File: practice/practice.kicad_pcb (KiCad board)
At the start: 2 copper layers, 27 x 22 mm, 5 parts

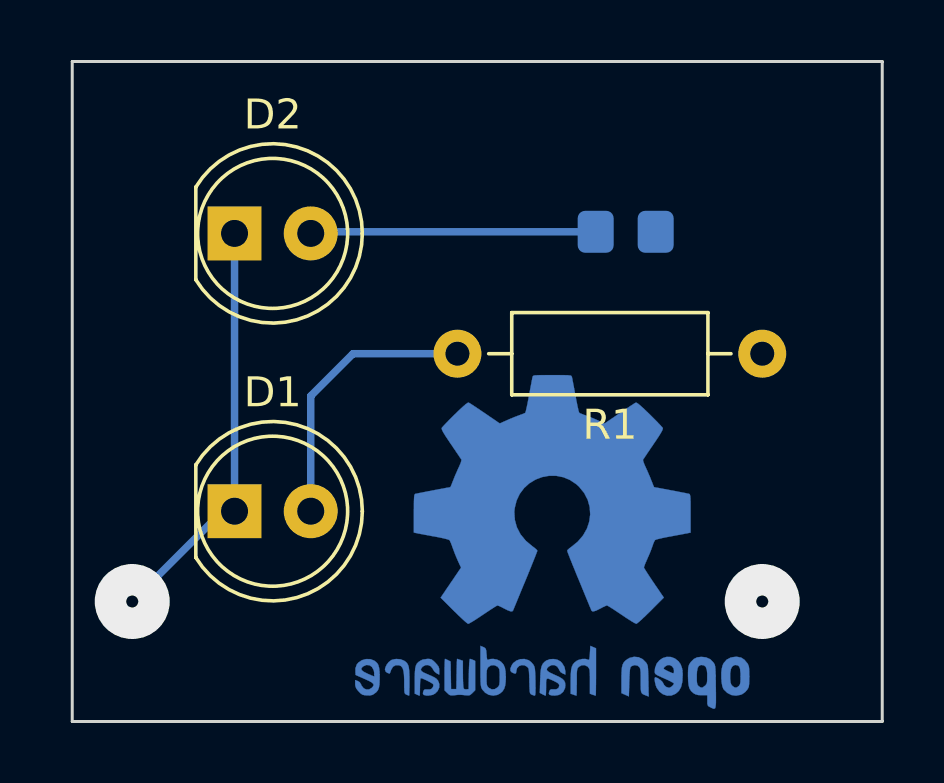
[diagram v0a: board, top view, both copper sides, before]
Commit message: 新增'UNO V3'資料夾 新增'learning project'資料夾
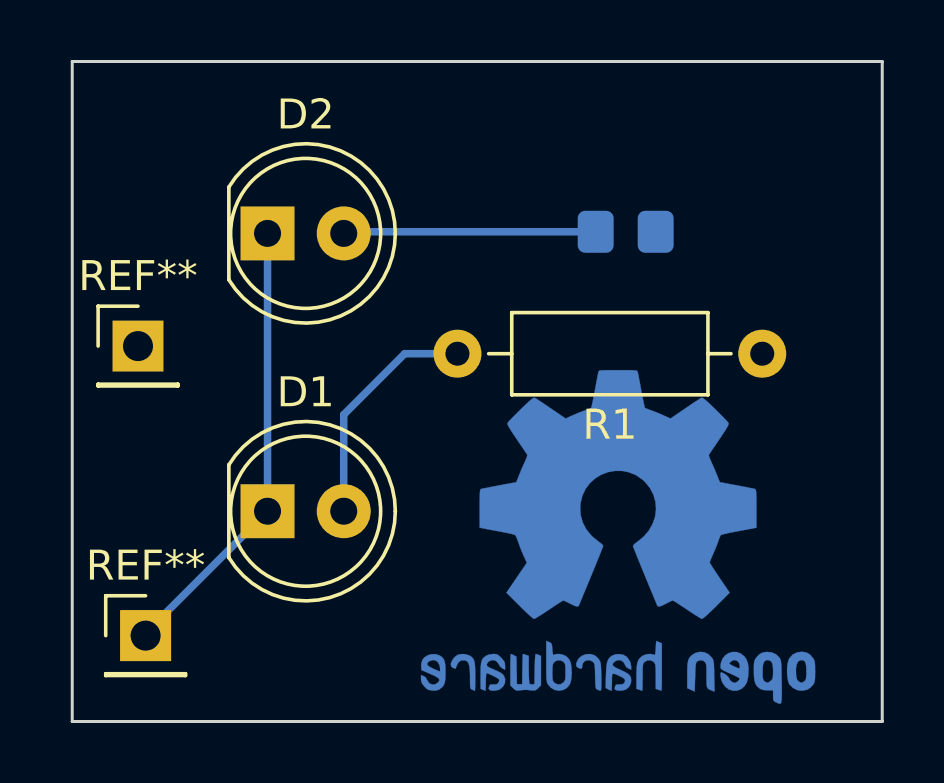
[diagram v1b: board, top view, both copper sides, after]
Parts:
- added REF**: PinHeader_1x01_P2.54mm_Vertical, Connector_PinHeader_2.54mm:PinHeader_1x01_P2.54mm_Vertical, F.Cu at (139.4, 88.1)
- added REF**: PinHeader_1x01_P2.54mm_Vertical, Connector_PinHeader_2.54mm:PinHeader_1x01_P2.54mm_Vertical, F.Cu at (139.2, 78.5)
- moved REF** 2.20 mm to (155.2, 84.8)
- moved D1 1.10 mm to (143.5, 84.0)
- moved D2 1.10 mm to (143.5, 74.7)
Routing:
- net Net-(D1-Pad2): track 9.61 -> 7.85 mm
- net VCC: track 14.2 -> 15.1 mm, vias 1 -> 0
- net GND: vias 1 -> 0
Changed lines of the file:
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@@
   (net 3 "GND")
   (net 4 "Net-(D2-Pad2)")
+  (footprint "Connector_PinHeader_2.54mm:PinHeader_1x01_P2.54mm_Vertical" (layer "F.Cu")
+    (at 139.446 88.138)
+    (descr "Through hole straight pin header, 1x01, 2.54mm pitch, single row")
+    (tags "Through hole pin header THT 1x01 2.54mm single row")
+    (attr through_hole)
+    (fp_text reference "REF**" (at 0 -2.33) (layer "F.SilkS")
+      (effects (font (size 1 1) (thickness 0.15)))
+    )
+    (fp_text value "PinHeader_1x01_P2.54mm_Vertical" (at 0 2.33) (layer "F.Fab")
+      (effects (font (size 1 1) (thickness 0.15)))
+    )
+    (fp_text user "${REFERENCE}" (at 0 0 90) (layer "F.Fab")
+      (effects (font (size 1 1) (thickness 0.15)))
+    )
+    (fp_line (start -1.33 1.27) (end -1.33 1.33) (layer "F.SilkS") (width 0.12))
+    (fp_line (start -1.33 0) (end -1.33 -1.33) (layer "F.SilkS") (width 0.12))
+    (fp_line (start 1.33 1.27) (end 1.33 1.33) (layer "F.SilkS") (width 0.12))
+    (fp_line (start -1.33 1.33) (end 1.33 1.33) (layer "F.SilkS") (width 0.12))
+    (fp_line (start -1.33 1.27) (end 1.33 1.27) (layer "F.SilkS") (width 0.12))
+    (fp_line (start -1.33 -1.33) (end 0 -1.33) (layer "F.SilkS") (width 0.12))
+    (fp_line (start 1.8 -1.8) (end -1.8 -1.8) (layer "F.CrtYd") (width 0.05))
+    (fp_line (start 1.8 1.8) (end 1.8 -1.8) (layer "F.CrtYd") (width 0.05))
+    (fp_line (start -1.8 -1.8) (end -1.8 1.8) (layer "F.CrtYd") (width 0.05))
+    (fp_line (start -1.8 1.8) (end 1.8 1.8) (layer "F.CrtYd") (width 0.05))
+    (fp_line (start -0.635 -1.27) (end 1.27 -1.27) (layer "F.Fab") (width 0.1))
+    (fp_line (start 1.27 1.27) (end -1.27 1.27) (layer "F.Fab") (width 0.1))
+    (fp_line (start -1.27 1.27) (end -1.27 -0.635) (layer "F.Fab") (width 0.1))
+    (fp_line (start -1.27 -0.635) (end -0.635 -1.27) (layer "F.Fab") (width 0.1))
+    (fp_line (start 1.27 -1.27) (end 1.27 1.27) (layer "F.Fab") (width 0.1))
+    (pad "1" thru_hole rect (at 0 0) (size 1.7 1.7) (drill 1) (layers *.Cu *.Mask)
+      (net 1 "VCC"))
+    (model "${KICAD6_3DMODEL_DIR}/Connector_PinHeader_2.54mm.3dshapes/PinHeader_1x01_P2.54mm_Vertical.wrl"
+      (offset (xyz 0 0 0))
+      (scale (xyz 1 1 1))
+      (rotate (xyz 0 0 0))
+    )
+  )
   (footprint "Resistor_THT:R_Axial_DIN0207_L6.3mm_D2.5mm_P10.16mm_Horizontal" (layer "F.Cu")
     (at 160 78.74 180)
@@
   )
   (footprint "LED_THT:LED_D5.0mm" (layer "F.Cu")
-    (at 142.41 74.73)
+    (at 143.51 74.73)
     (descr "LED, diameter 5.0mm, 2 pins, http://cdn-reichelt.de/documents/datenblatt/A500/LL-504BC2E-009.pdf")
     (tags "LED diameter 5.0mm 2 pins")
@@
     )
   )
+  (footprint "Connector_PinHeader_2.54mm:PinHeader_1x01_P2.54mm_Vertical" (layer "F.Cu")
+    (at 139.192 78.486)
+    (descr "Through hole straight pin header, 1x01, 2.54mm pitch, single row")
+    (tags "Through hole pin header THT 1x01 2.54mm single row")
+    (attr through_hole)
+    (fp_text reference "REF**" (at 0 -2.33) (layer "F.SilkS")
+      (effects (font (size 1 1) (thickness 0.15)))
+    )
+    (fp_text value "PinHeader_1x01_P2.54mm_Vertical" (at 0 2.33) (layer "F.Fab")
+      (effects (font (size 1 1) (thickness 0.15)))
+    )
+    (fp_text user "${REFERENCE}" (at 0 0 90) (layer "F.Fab")
+      (effects (font (size 1 1) (thickness 0.15)))
+    )
+    (fp_line (start -1.33 1.27) (end -1.33 1.33) (layer "F.SilkS") (width 0.12))
+    (fp_line (start -1.33 0) (end -1.33 -1.33) (layer "F.SilkS") (width 0.12))
+    (fp_line (start 1.33 1.27) (end 1.33 1.33) (layer "F.SilkS") (width 0.12))
+    (fp_line (start -1.33 1.33) (end 1.33 1.33) (layer "F.SilkS") (width 0.12))
+    (fp_line (start -1.33 1.27) (end 1.33 1.27) (layer "F.SilkS") (width 0.12))
+    (fp_line (start -1.33 -1.33) (end 0 -1.33) (layer "F.SilkS") (width 0.12))
+    (fp_line (start 1.8 -1.8) (end -1.8 -1.8) (layer "F.CrtYd") (width 0.05))
+    (fp_line (start 1.8 1.8) (end 1.8 -1.8) (layer "F.CrtYd") (width 0.05))
+    (fp_line (start -1.8 -1.8) (end -1.8 1.8) (layer "F.CrtYd") (width 0.05))
+    (fp_line (start -1.8 1.8) (end 1.8 1.8) (layer "F.CrtYd") (width 0.05))
+    (fp_line (start -0.635 -1.27) (end 1.27 -1.27) (layer "F.Fab") (width 0.1))
+    (fp_line (start 1.27 1.27) (end -1.27 1.27) (layer "F.Fab") (width 0.1))
+    (fp_line (start -1.27 1.27) (end -1.27 -0.635) (layer "F.Fab") (width 0.1))
+    (fp_line (start -1.27 -0.635) (end -0.635 -1.27) (layer "F.Fab") (width 0.1))
+    (fp_line (start 1.27 -1.27) (end 1.27 1.27) (layer "F.Fab") (width 0.1))
+    (pad "1" thru_hole rect (at 0 0) (size 1.7 1.7) (drill 1) (layers *.Cu *.Mask)
+      (net 3 "GND"))
+    (model "${KICAD6_3DMODEL_DIR}/Connector_PinHeader_2.54mm.3dshapes/PinHeader_1x01_P2.54mm_Vertical.wrl"
+      (offset (xyz 0 0 0))
+      (scale (xyz 1 1 1))
+      (rotate (xyz 0 0 0))
+    )
+  )
   (footprint "LED_THT:LED_D5.0mm" (layer "F.Cu")
-    (at 142.41 83.99)
+    (at 143.51 83.99)
     (descr "LED, diameter 5.0mm, 2 pins, http://cdn-reichelt.de/documents/datenblatt/A500/LL-504BC2E-009.pdf")
     (tags "LED diameter 5.0mm 2 pins")
@@
   )
   (footprint "Symbol:OSHW-Logo2_14.6x12mm_Copper" (layer "B.Cu")
-    (at 153 85 180)
+    (at 155.194 84.836 180)
     (descr "Open Source Hardware Symbol")
     (tags "Logo Symbol OSHW")
@@
       (xy 164 69)
     ) (layer "Edge.Cuts") (width 0.1) (fill none))
-  (segment (start 142.58 83.82) (end 142.41 83.99) (width 0.25) (layer "F.Cu") (net 1))
-  (via (at 139 87) (size 2.5) (drill 0.4) (layers "F.Cu" "B.Cu") (remove_unused_layers) (keep_end_layers) (free) (net 1))
-  (segment (start 142.01 83.99) (end 142.41 83.99) (width 0.25) (layer "B.Cu") (net 1))
-  (segment (start 139 87) (end 142.01 83.99) (width 0.25) (layer "B.Cu") (net 1))
-  (segment (start 142.41 74.73) (end 142.41 83.99) (width 0.25) (layer "B.Cu") (net 1))
-  (segment (start 144.95 80.15) (end 146.36 78.74) (width 0.25) (layer "B.Cu") (net 2))
-  (segment (start 144.95 83.99) (end 144.95 80.15) (width 0.25) (layer "B.Cu") (net 2))
-  (segment (start 146.36 78.74) (end 149.84 78.74) (width 0.25) (layer "B.Cu") (net 2))
-  (segment (start 149.63 78.95) (end 149.84 78.74) (width 0.25) (layer "B.Cu") (net 2))
-  (via (at 160 87) (size 2.5) (drill 0.4) (layers "F.Cu" "B.Cu") (remove_unused_layers) (keep_end_layers) (free) (net 3))
-  (segment (start 145.531717 74.676) (end 145.267858 74.412141) (width 0.25) (layer "B.Cu") (net 4))
+  (segment (start 139.446 88.054) (end 139.446 88.138) (width 0.25) (layer "B.Cu") (net 1))
+  (segment (start 143.51 83.99) (end 139.446 88.054) (width 0.25) (layer "B.Cu") (net 1))
+  (segment (start 143.51 74.73) (end 143.51 83.99) (width 0.25) (layer "B.Cu") (net 1))
+  (segment (start 148.082 78.74) (end 146.05 80.772) (width 0.25) (layer "B.Cu") (net 2))
+  (segment (start 146.05 80.772) (end 146.05 83.99) (width 0.25) (layer "B.Cu") (net 2))
+  (segment (start 148.082 78.74) (end 149.84 78.74) (width 0.25) (layer "B.Cu") (net 2))
   (segment (start 154.448 74.676) (end 145.531717 74.676) (width 0.25) (layer "B.Cu") (net 4))
   (zone (net 3) (net_name "GND") (layer "B.Cu") (hatch edge 0.508)
     (connect_pads (clearance 0.508))
     (min_thickness 0.254) (filled_areas_thickness no)
-    (fill yes (thermal_gap 0.508) (thermal_bridge_width 0.508) (smoothing fillet) (radius 3) (island_removal_mode 2) (island_area_min 10))
+    (fill yes (thermal_gap 0.508) (thermal_bridge_width 0.508) (smoothing fillet) (radius 2) (island_removal_mode 2) (island_area_min 0))
     (polygon
       (pts
-        (xy 164 91)
-        (xy 137 91)
+        (xy 163.99 69.01)
+        (xy 163.99 91.01)
+        (xy 137 90.98)
         (xy 137 69)
-        (xy 164 69)
       )
     )
